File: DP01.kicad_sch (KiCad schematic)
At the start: 12 parts

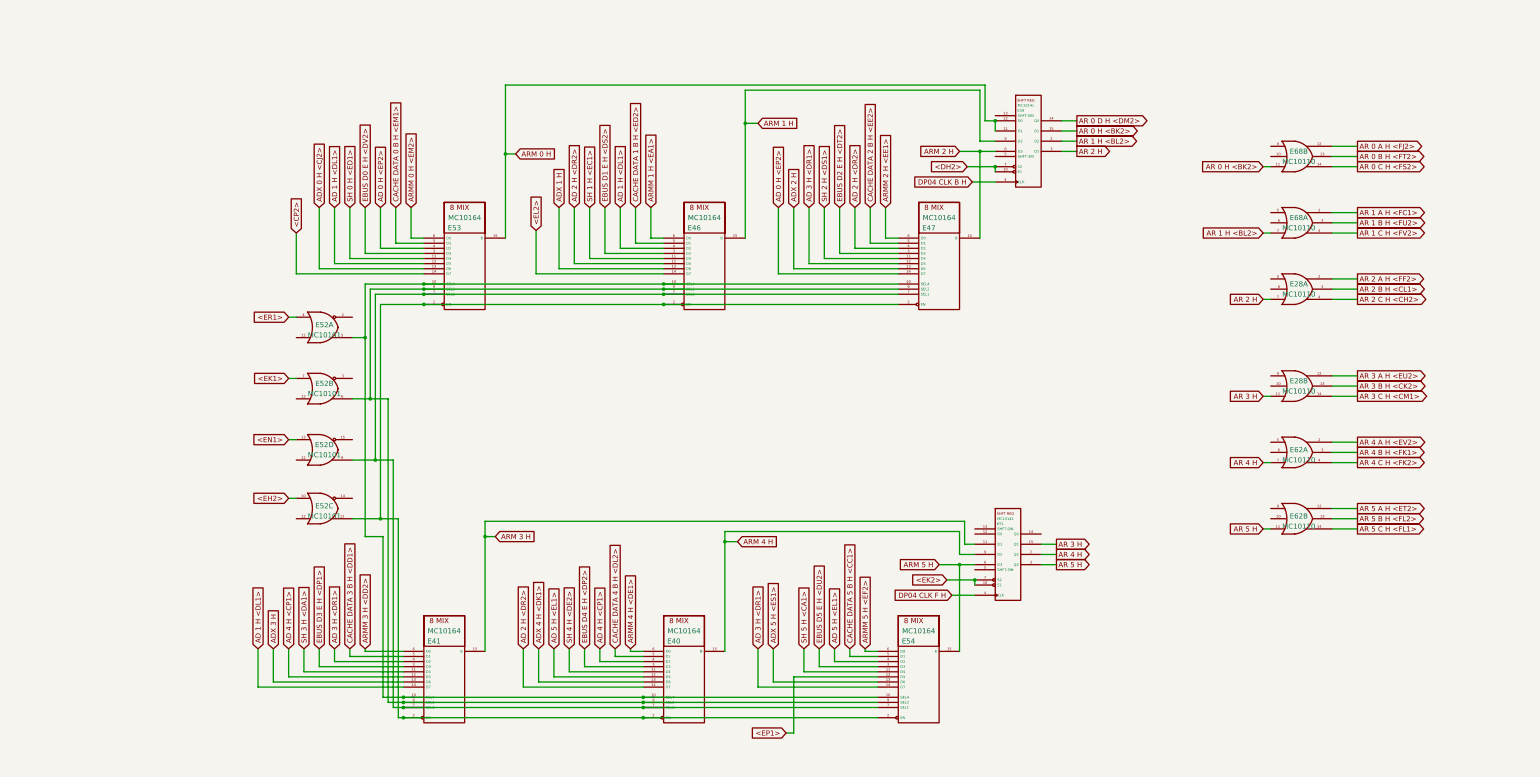
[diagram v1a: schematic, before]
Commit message: Fix a bunch of typos, add ${N} macros for slot specific net names
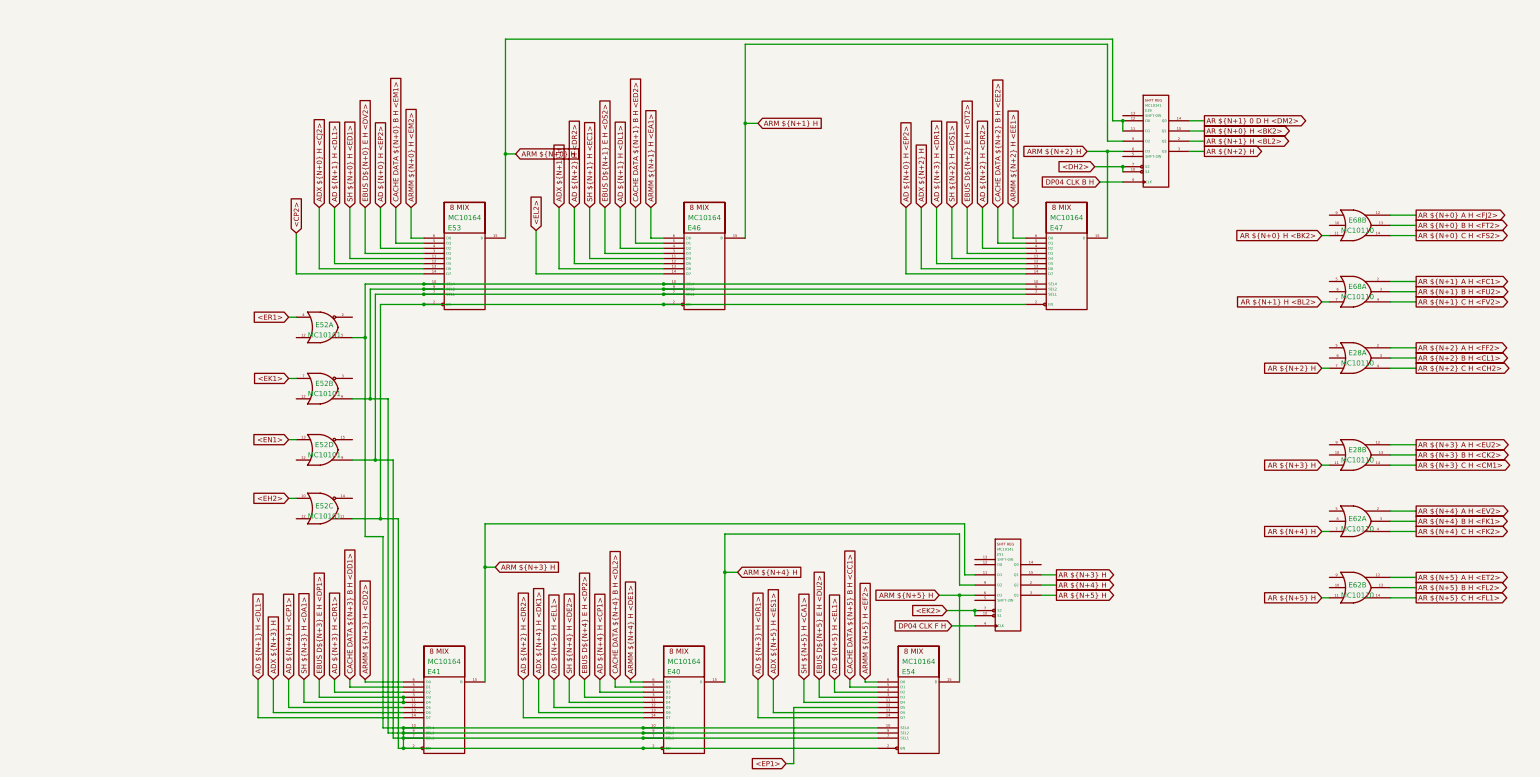
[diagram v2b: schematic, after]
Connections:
- net SH 3 H <DA1> is gone; now on net EBUS D${N+3} E H <DP1>: E41.11 (D4)
- net at E40.7 (SEL1), E41.7 (SEL1), E46.7 (SEL1)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: now also E40.10 (SEL4), E40.2 (EN), E40.9 (SEL2), E41.10 (SEL4), E41.2 (EN), E41.9 (SEL2), E46.10 (SEL4), E46.2 (EN), E46.9 (SEL2), E47.10 (SEL4), E47.2 (EN), E47.9 (SEL2), E52.11 (Cout), E52.5 (Aout), E52.6 (Bout), E53.10 (SEL4), E53.2 (EN), E53.9 (SEL2), E54.10 (SEL4), E54.2 (EN), E54.9 (SEL2)
- net AD 0 H <EP2> renamed AD ${N+0} H <EP2>
- net AD 1 H <DL1> renamed AD ${N+1} H <DL1>
- net AD 2 H <DR2> renamed AD ${N+2} H <DR2>
- net AD 3 H <DR1> renamed AD ${N+3} H <DR1>
- net AD 4 H <CP1> renamed AD ${N+4} H <CP1>
- net AD 5 H <EL1> renamed AD ${N+5} H <EL1>
- net ADX 0 H <CJ2> renamed ADX ${N+0} H <CJ2>
- net ADX 1 H renamed ADX ${N+1} H
- net ADX 2 H renamed ADX ${N+2} H
- net ADX 3 H renamed ADX ${N+3} H
- net ADX 4 H <DK1> renamed ADX ${N+4} H <DK1>
- net ADX 5 H <ES1> renamed ADX ${N+5} H <ES1>
- net AR 0 A H <FJ2> renamed AR ${N+0} A H <FJ2>
- net AR 0 B H <FT2> renamed AR ${N+0} B H <FT2>
- net AR 0 C H <FS2> renamed AR ${N+0} C H <FS2>
- net AR 0 D H <DM2> renamed AR ${N+1} 0 D H <DM2>
- net AR 0 H <BK2> renamed AR ${N+0} H <BK2>
- net AR 1 A H <FC1> renamed AR ${N+1} A H <FC1>
- net AR 1 B H <FU2> renamed AR ${N+1} B H <FU2>
- net AR 1 C H <FV2> renamed AR ${N+1} C H <FV2>
- net AR 1 H <BL2> renamed AR ${N+1} H <BL2>
- net AR 2 A H <FF2> renamed AR ${N+2} A H <FF2>
- net AR 2 B H <CL1> renamed AR ${N+2} B H <CL1>
- net AR 2 C H <CH2> renamed AR ${N+2} C H <CH2>
- net AR 2 H renamed AR ${N+2} H
- net AR 3 A H <EU2> renamed AR ${N+3} A H <EU2>
- net AR 3 B H <CK2> renamed AR ${N+3} B H <CK2>
- net AR 3 C H <CM1> renamed AR ${N+3} C H <CM1>
- net AR 3 H renamed AR ${N+3} H
- net AR 4 A H <EV2> renamed AR ${N+4} A H <EV2>
- net AR 4 B H <FK1> renamed AR ${N+4} B H <FK1>
- net AR 4 C H <FK2> renamed AR ${N+4} C H <FK2>
- net AR 4 H renamed AR ${N+4} H
- net AR 5 A H <ET2> renamed AR ${N+5} A H <ET2>
- net AR 5 B H <FL2> renamed AR ${N+5} B H <FL2>
- net AR 5 C H <FL1> renamed AR ${N+5} C H <FL1>
- net AR 5 H renamed AR ${N+5} H
- net ARM 0 H renamed ARM ${N+0} H
- net ARM 1 H renamed ARM ${N+1} H
- net ARM 2 H renamed ARM ${N+2} H
- net ARM 3 H renamed ARM ${N+3} H
- net ARM 4 H renamed ARM ${N+4} H
- net ARM 5 H renamed ARM ${N+5} H
- net ARMM 0 H <EM2> renamed ARMM ${N+0} H <EM2>
- net ARMM 1 H <EA1> renamed ARMM ${N+1} H <EA1>
- net ARMM 2 H <EE1> renamed ARMM ${N+2} H <EE1>
- net ARMM 3 H <DD2> renamed ARMM ${N+3} H <DD2>
- net ARMM 4 H <DE1> renamed ARMM ${N+4} H <DE1>
- net ARMM 5 H <EF2> renamed ARMM ${N+5} H <EF2>
- net CACHE DATA 0 B H <EM1> renamed CACHE DATA ${N+0} B H <EM1>
- net CACHE DATA 1 B H <ED2> renamed CACHE DATA ${N+1} B H <ED2>
- net CACHE DATA 2 B H <EE2> renamed CACHE DATA ${N+2} B H <EE2>
- net CACHE DATA 3 B H <DD1> renamed CACHE DATA ${N+3} B H <DD1>
- net CACHE DATA 4 B H <DL2> renamed CACHE DATA ${N+4} B H <DL2>
- net CACHE DATA 5 B H <CC1> renamed CACHE DATA ${N+5} B H <CC1>
- net EBUS D0 E H <DV2> renamed EBUS D${N+0} E H <DV2>
- net EBUS D1 E H <DS2> renamed EBUS D${N+1} E H <DS2>
- net EBUS D2 E H <DT2> renamed EBUS D${N+2} E H <DT2>
- net EBUS D3 E H <DP1> renamed EBUS D${N+3} E H <DP1>
- net EBUS D4 E H <DP2> renamed EBUS D${N+4} E H <DP2>
- net EBUS D5 E H <DU2> renamed EBUS D${N+5} E H <DU2>
- net SH 0 H <ED1> renamed SH ${N+0} H <ED1>
- net SH 1 H <EC1> renamed SH ${N+1} H <EC1>
- net SH 2 H <DS1> renamed SH ${N+2} H <DS1>
- net SH 4 H <DE2> renamed SH ${N+4} H <DE2>
- net SH 5 H <CA1> renamed SH ${N+5} H <CA1>
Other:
- moved on the sheet: E28A, E28B, E39, E40, E41, E47, E51, E54, E62A, E62B, E68A, E68B

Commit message: Define multi-selector per-slot signals in DP01 (still have to do DP2-4)
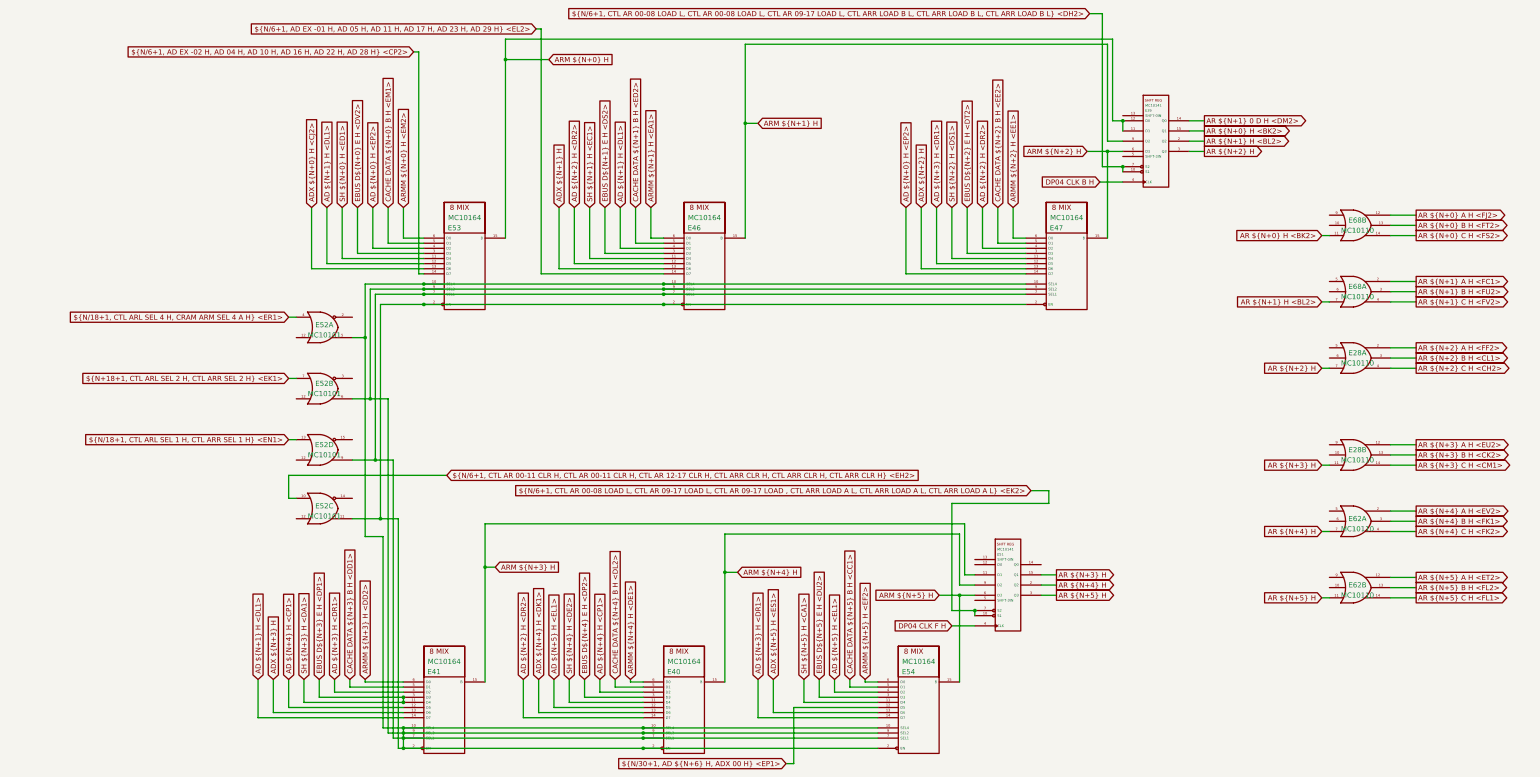
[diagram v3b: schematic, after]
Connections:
- net <CP2> renamed ${N/6+1, AD EX -02 H, AD 04 H, AD 10 H, AD 16 H, AD 22 H, AD 28 H} <CP2>
- net <DH2> renamed ${N/6+1, CTL AR 00-08 LOAD L, CTL AR 00-08 LOAD L, CTL AR 09-17 LOAD L, CTL ARR LOAD B L, CTL ARR LOAD B L, CTL ARR LOAD B L} <DH2>
- net <EH2> renamed ${N/6+1, CTL AR 00-11 CLR H, CTL AR 00-11 CLR H, CTL AR 12-17 CLR H, CTL ARR CLR H, CTL ARR CLR H, CTL ARR CLR H} <EH2>
- net <EK1> renamed ${N+18+1, CTL ARL SEL 2 H, CTL ARR SEL 2 H} <EK1>
- net <EK2> renamed ${N/6+1, CTL AR 00-08 LOAD L, CTL AR 09-17 LOAD L, CTL AR 09-17 LOAD , CTL ARR LOAD A L, CTL ARR LOAD A L, CTL ARR LOAD A L} <EK2>
- net <EL2> renamed ${N/6+1, AD EX -01 H, AD 05 H, AD 11 H, AD 17 H, AD 23 H, AD 29 H} <EL2>
- net <EN1> renamed ${N/18+1, CTL ARL SEL 1 H, CTL ARR SEL 1 H} <EN1>
- net <EP1> renamed ${N/30+1, AD ${N+6} H, ADX 00 H} <EP1>
- net <ER1> renamed ${N/18+1, CTL ARL SEL 4 H, CRAM ARM SEL 4 A H} <ER1>

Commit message: Fix up undefined signal names on J1 pins
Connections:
- net ${N+18+1, CTL ARL SEL 2 H, CTL ARR SEL 2 H} <EK1> renamed ${N/18+1, CTL ARL SEL 2 H, CTL ARR SEL 2 H} <EK1>
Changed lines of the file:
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@@
     )
   )
-  (global_label "${N+18+1, CTL ARL SEL 2 H, CTL ARR SEL 2 H} <EK1>" (shape input) (at 86.36 114.3 180) (fields_autoplaced)
+  (global_label "${N{slash}18+1, CTL ARL SEL 2 H, CTL ARR SEL 2 H} <EK1>" (shape input)
+    (at 86.36 114.3 0) (fields_autoplaced)
     (effects (font (size 1.27 1.27)) (justify right))
-    (property "Intersheet References" "${INTERSHEET_REFS}" (id 0) (at 28.9136 114.2206 0)
+    (property "Intersheet References" "${INTERSHEET_REFS}" (id 0) (at 23.7731 114.2206 0)
       (effects (font (size 1.27 1.27)) (justify right) hide)
     )

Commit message: Remove "slash" in several places as an experiment. it did not work.
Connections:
- net ${N/18+1, CTL ARL SEL 1 H, CTL ARR SEL 1 H} <EN1> renamed ${N/18+1, CTL ARL SEL 1 H, CTL ARR SEL 1 H} <EN1>
- net ${N/18+1, CTL ARL SEL 2 H, CTL ARR SEL 2 H} <EK1> renamed ${N/18+1, CTL ARL SEL 2 H, CTL ARR SEL 2 H} <EK1>
- net ${N/18+1, CTL ARL SEL 4 H, CRAM ARM SEL 4 A H} <ER1> renamed ${N/18+1, CTL ARL SEL 4 H, CRAM ARM SEL 4 A H} <ER1>
- net ${N/30+1, AD ${N+6} H, ADX 00 H} <EP1> renamed ${N/30+1, AD ${N+6} H, ADX 00 H} <EP1>
- net ${N/6+1, AD EX -01 H, AD 05 H, AD 11 H, AD 17 H, AD 23 H, AD 29 H} <EL2> renamed ${N/6+1, AD EX -01 H, AD 05 H, AD 11 H, AD 17 H, AD 23 H, AD 29 H} <EL2>
- net ${N/6+1, AD EX -02 H, AD 04 H, AD 10 H, AD 16 H, AD 22 H, AD 28 H} <CP2> renamed ${N/6+1, AD EX -02 H, AD 04 H, AD 10 H, AD 16 H, AD 22 H, AD 28 H} <CP2>
- net ${N/6+1, CTL AR 00-08 LOAD L, CTL AR 00-08 LOAD L, CTL AR 09-17 LOAD L, CTL ARR LOAD B L, CTL ARR LOAD B L, CTL ARR LOAD B L} <DH2> renamed ${N/6+1, CTL AR 00-08 LOAD L, CTL AR 00-08 LOAD L, CTL AR 09-17 LOAD L, CTL ARR LOAD B L, CTL ARR LOAD B L, CTL ARR LOAD B L} <DH2>
- net ${N/6+1, CTL AR 00-08 LOAD L, CTL AR 09-17 LOAD L, CTL AR 09-17 LOAD , CTL ARR LOAD A L, CTL ARR LOAD A L, CTL ARR LOAD A L} <EK2> renamed ${N/6+1, CTL AR 00-08 LOAD L, CTL AR 09-17 LOAD L, CTL AR 09-17 LOAD , CTL ARR LOAD A L, CTL ARR LOAD A L, CTL ARR LOAD A L} <EK2>
- net ${N/6+1, CTL AR 00-11 CLR H, CTL AR 00-11 CLR H, CTL AR 12-17 CLR H, CTL ARR CLR H, CTL ARR CLR H, CTL ARR CLR H} <EH2> renamed ${N/6+1, CTL AR 00-11 CLR H, CTL AR 00-11 CLR H, CTL AR 12-17 CLR H, CTL ARR CLR H, CTL ARR CLR H, CTL ARR CLR H} <EH2>
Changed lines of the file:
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@@
     )
   )
-  (global_label "${N{slash}18+1, CTL ARL SEL 4 H, CRAM ARM SEL 4 A H} <ER1>" (shape input)
+  (global_label "${N/18+1, CTL ARL SEL 4 H, CRAM ARM SEL 4 A H} <ER1>" (shape input)
     (at 86.36 99.06 0) (fields_autoplaced)
     (effects (font (size 1.27 1.27)) (justify right))
@@
     )
   )
-  (global_label "${N{slash}30+1, AD ${N+6} H, ADX 00 H} <EP1>" (shape input) (at 210.185 210.185 180) (fields_autoplaced)
+  (global_label "${N/30+1, AD ${N+6} H, ADX 00 H} <EP1>" (shape input) (at 210.185 210.185 180) (fields_autoplaced)
     (effects (font (size 1.27 1.27)) (justify right))
     (property "Intersheet References" "${INTERSHEET_REFS}" (id 0) (at 158.8467 210.1056 0)
@@
     )
   )
-  (global_label "${N{slash}6+1, AD EX -02 H, AD 04 H, AD 10 H, AD 16 H, AD 22 H, AD 28 H} <CP2>" (shape input)
+  (global_label "${N/6+1, AD EX -02 H, AD 04 H, AD 10 H, AD 16 H, AD 22 H, AD 28 H} <CP2>" (shape input)
     (at 117.475 33.02 0) (fields_autoplaced)
     (effects (font (size 1.27 1.27)) (justify right))
@@
     )
   )
-  (global_label "${N{slash}6+1, AD EX -01 H, AD 05 H, AD 11 H, AD 17 H, AD 23 H, AD 29 H} <EL2>" (shape input)
+  (global_label "${N/6+1, AD EX -01 H, AD 05 H, AD 11 H, AD 17 H, AD 23 H, AD 29 H} <EL2>" (shape input)
     (at 147.955 27.305 0) (fields_autoplaced)
     (effects (font (size 1.27 1.27)) (justify right))
@@
     )
   )
-  (global_label "${N{slash}18+1, CTL ARL SEL 1 H, CTL ARR SEL 1 H} <EN1>" (shape input)
-    (at 86.36 129.54 0) (fields_autoplaced)
+  (global_label "${N/18+1, CTL ARL SEL 1 H, CTL ARR SEL 1 H} <EN1>" (shape input) (at 86.36 129.54 180) (fields_autoplaced)
     (effects (font (size 1.27 1.27)) (justify right))
     (property "Intersheet References" "${INTERSHEET_REFS}" (id 0) (at 23.7126 129.4606 0)
@@
     )
   )
-  (global_label "${N{slash}6+1, CTL AR 00-08 LOAD L, CTL AR 00-08 LOAD L, CTL AR 09-17 LOAD L, CTL ARR LOAD B L, CTL ARR LOAD B L, CTL ARR LOAD B L} <DH2>" (shape input)
+  (global_label "${N/6+1, CTL AR 00-08 LOAD L, CTL AR 00-08 LOAD L, CTL AR 09-17 LOAD L, CTL ARR LOAD B L, CTL ARR LOAD B L, CTL ARR LOAD B L} <DH2>" (shape input)
     (at 285.75 23.495 0) (fields_autoplaced)
     (effects (font (size 1.27 1.27)) (justify right))
@@
     )
   )
-  (global_label "${N{slash}18+1, CTL ARL SEL 2 H, CTL ARR SEL 2 H} <EK1>" (shape input)
-    (at 86.36 114.3 0) (fields_autoplaced)
+  (global_label "${N/18+1, CTL ARL SEL 2 H, CTL ARR SEL 2 H} <EK1>" (shape input) (at 86.36 114.3 180) (fields_autoplaced)
     (effects (font (size 1.27 1.27)) (justify right))
     (property "Intersheet References" "${INTERSHEET_REFS}" (id 0) (at 23.7731 114.2206 0)
@@
     )
   )
-  (global_label "${N{slash}6+1, CTL AR 00-11 CLR H, CTL AR 00-11 CLR H, CTL AR 12-17 CLR H, CTL ARR CLR H, CTL ARR CLR H, CTL ARR CLR H} <EH2>" (shape input)
+  (global_label "${N/6+1, CTL AR 00-11 CLR H, CTL AR 00-11 CLR H, CTL AR 12-17 CLR H, CTL ARR CLR H, CTL ARR CLR H, CTL ARR CLR H} <EH2>" (shape input)
     (at 125.73 138.43 0) (fields_autoplaced)
     (effects (font (size 1.27 1.27)) (justify left))
@@
     )
   )
-  (global_label "${N{slash}6+1, CTL AR 00-08 LOAD L, CTL AR 09-17 LOAD L, CTL AR 09-17 LOAD , CTL ARR LOAD A L, CTL ARR LOAD A L, CTL ARR LOAD A L} <EK2>" (shape input)
+  (global_label "${N/6+1, CTL AR 00-08 LOAD L, CTL AR 09-17 LOAD L, CTL AR 09-17 LOAD , CTL ARR LOAD A L, CTL ARR LOAD A L, CTL ARR LOAD A L} <EK2>" (shape input)
     (at 271.145 142.24 0) (fields_autoplaced)
     (effects (font (size 1.27 1.27)) (justify right))

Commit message: Parser is greedily eating characters up to next "}" instead of following nesting. Fix lowercase "h" found in some signal names. Add error message stuff for signal name syntax errors.
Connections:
- net ${N/18+1, CTL ARL SEL 1 H, CTL ARR SEL 1 H} <EN1> renamed ${N/18+1,CTL ARL SEL 1 H,CTL ARR SEL 1 H} <EN1>
- net ${N/18+1, CTL ARL SEL 2 H, CTL ARR SEL 2 H} <EK1> renamed ${N/18+1,CTL ARL SEL 2 H,CTL ARR SEL 2 H} <EK1>
- net ${N/18+1, CTL ARL SEL 4 H, CRAM ARM SEL 4 A H} <ER1> renamed ${N/18+1,CTL ARL SEL 4 H,CRAM ARM SEL 4 A H} <ER1>
- net ${N/30+1, AD ${N+6} H, ADX 00 H} <EP1> renamed ${N/30+1,AD ${N+6} H,ADX 00 H} <EP1>
- net ${N/6+1, AD EX -01 H, AD 05 H, AD 11 H, AD 17 H, AD 23 H, AD 29 H} <EL2> renamed ${N/6+1,AD EX -01 H,AD 05 H,AD 11 H,AD 17 H,AD 23 H,AD 29 H} <EL2>
- net ${N/6+1, AD EX -02 H, AD 04 H, AD 10 H, AD 16 H, AD 22 H, AD 28 H} <CP2> renamed ${N/6+1,AD EX -02 H,AD 04 H,AD 10 H,AD 16 H,AD 22 H,AD 28 H} <CP2>
- net ${N/6+1, CTL AR 00-08 LOAD L, CTL AR 00-08 LOAD L, CTL AR 09-17 LOAD L, CTL ARR LOAD B L, CTL ARR LOAD B L, CTL ARR LOAD B L} <DH2> renamed ${N/6+1,CTL AR 00-08 LOAD L,CTL AR 00-08 LOAD L,CTL AR 09-17 LOAD L,CTL ARR LOAD B L,CTL ARR LOAD B L,CTL ARR LOAD B L} <DH2>
- net ${N/6+1, CTL AR 00-08 LOAD L, CTL AR 09-17 LOAD L, CTL AR 09-17 LOAD , CTL ARR LOAD A L, CTL ARR LOAD A L, CTL ARR LOAD A L} <EK2> renamed ${N/6+1,CTL AR 00-08 LOAD L,CTL AR 09-17 LOAD L,CTL AR 09-17 LOAD ,CTL ARR LOAD A L,CTL ARR LOAD A L,CTL ARR LOAD A L} <EK2>
- net ${N/6+1, CTL AR 00-11 CLR H, CTL AR 00-11 CLR H, CTL AR 12-17 CLR H, CTL ARR CLR H, CTL ARR CLR H, CTL ARR CLR H} <EH2> renamed ${N/6+1,CTL AR 00-11 CLR H,CTL AR 00-11 CLR H,CTL AR 12-17 CLR H,CTL ARR CLR H,CTL ARR CLR H,CTL ARR CLR H} <EH2>
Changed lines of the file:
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@@
     )
   )
-  (global_label "${N/18+1, CTL ARL SEL 4 H, CRAM ARM SEL 4 A H} <ER1>" (shape input)
+  (global_label "${N/18+1,CTL ARL SEL 4 H,CRAM ARM SEL 4 A H} <ER1>" (shape input)
     (at 86.36 99.06 0) (fields_autoplaced)
     (effects (font (size 1.27 1.27)) (justify right))
@@
     )
   )
-  (global_label "${N/30+1, AD ${N+6} H, ADX 00 H} <EP1>" (shape input) (at 210.185 210.185 180) (fields_autoplaced)
+  (global_label "${N/30+1,AD ${N+6} H,ADX 00 H} <EP1>" (shape input) (at 210.185 210.185 180) (fields_autoplaced)
     (effects (font (size 1.27 1.27)) (justify right))
     (property "Intersheet References" "${INTERSHEET_REFS}" (id 0) (at 158.8467 210.1056 0)
@@
     )
   )
-  (global_label "${N/6+1, AD EX -02 H, AD 04 H, AD 10 H, AD 16 H, AD 22 H, AD 28 H} <CP2>" (shape input)
+  (global_label "${N/6+1,AD EX -02 H,AD 04 H,AD 10 H,AD 16 H,AD 22 H,AD 28 H} <CP2>" (shape input)
     (at 117.475 33.02 0) (fields_autoplaced)
     (effects (font (size 1.27 1.27)) (justify right))
@@
     )
   )
-  (global_label "${N/6+1, AD EX -01 H, AD 05 H, AD 11 H, AD 17 H, AD 23 H, AD 29 H} <EL2>" (shape input)
+  (global_label "${N/6+1,AD EX -01 H,AD 05 H,AD 11 H,AD 17 H,AD 23 H,AD 29 H} <EL2>" (shape input)
     (at 147.955 27.305 0) (fields_autoplaced)
     (effects (font (size 1.27 1.27)) (justify right))
@@
     )
   )
-  (global_label "${N/18+1, CTL ARL SEL 1 H, CTL ARR SEL 1 H} <EN1>" (shape input) (at 86.36 129.54 180) (fields_autoplaced)
+  (global_label "${N/18+1,CTL ARL SEL 1 H,CTL ARR SEL 1 H} <EN1>" (shape input) (at 86.36 129.54 180) (fields_autoplaced)
     (effects (font (size 1.27 1.27)) (justify right))
     (property "Intersheet References" "${INTERSHEET_REFS}" (id 0) (at 23.7126 129.4606 0)
@@
     )
   )
-  (global_label "${N/6+1, CTL AR 00-08 LOAD L, CTL AR 00-08 LOAD L, CTL AR 09-17 LOAD L, CTL ARR LOAD B L, CTL ARR LOAD B L, CTL ARR LOAD B L} <DH2>" (shape input)
+  (global_label "${N/6+1,CTL AR 00-08 LOAD L,CTL AR 00-08 LOAD L,CTL AR 09-17 LOAD L,CTL ARR LOAD B L,CTL ARR LOAD B L,CTL ARR LOAD B L} <DH2>" (shape input)
     (at 285.75 23.495 0) (fields_autoplaced)
     (effects (font (size 1.27 1.27)) (justify right))
@@
     )
   )
-  (global_label "${N/18+1, CTL ARL SEL 2 H, CTL ARR SEL 2 H} <EK1>" (shape input) (at 86.36 114.3 180) (fields_autoplaced)
+  (global_label "${N/18+1,CTL ARL SEL 2 H,CTL ARR SEL 2 H} <EK1>" (shape input) (at 86.36 114.3 180) (fields_autoplaced)
     (effects (font (size 1.27 1.27)) (justify right))
     (property "Intersheet References" "${INTERSHEET_REFS}" (id 0) (at 23.7731 114.2206 0)
@@
     )
   )
-  (global_label "${N/6+1, CTL AR 00-11 CLR H, CTL AR 00-11 CLR H, CTL AR 12-17 CLR H, CTL ARR CLR H, CTL ARR CLR H, CTL ARR CLR H} <EH2>" (shape input)
+  (global_label "${N/6+1,CTL AR 00-11 CLR H,CTL AR 00-11 CLR H,CTL AR 12-17 CLR H,CTL ARR CLR H,CTL ARR CLR H,CTL ARR CLR H} <EH2>" (shape input)
     (at 125.73 138.43 0) (fields_autoplaced)
     (effects (font (size 1.27 1.27)) (justify left))
@@
     )
   )
-  (global_label "${N/6+1, CTL AR 00-08 LOAD L, CTL AR 09-17 LOAD L, CTL AR 09-17 LOAD , CTL ARR LOAD A L, CTL ARR LOAD A L, CTL ARR LOAD A L} <EK2>" (shape input)
+  (global_label "${N/6+1,CTL AR 00-08 LOAD L,CTL AR 09-17 LOAD L,CTL AR 09-17 LOAD ,CTL ARR LOAD A L,CTL ARR LOAD A L,CTL ARR LOAD A L} <EK2>" (shape input)
     (at 271.145 142.24 0) (fields_autoplaced)
     (effects (font (size 1.27 1.27)) (justify right))
